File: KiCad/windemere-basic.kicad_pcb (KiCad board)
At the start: 2 copper layers, 246.4 x 157.5 mm, 51 parts, among them J2 Barrel_Jack, SW1 SW_SPDT, SW2 Push_Button, U1 WD65C02, U2 28C256, U3 62256, U4 WD65C22, U5 HD44780U, U6 74HC00, U7 MM74C922, U8 L7805, X1 1MHz

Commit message: pcb
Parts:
- R7: footprint Resistor_THT:R_Axial_DIN0207_L6.3mm_D2.5mm_P10.16mm_Horizontal -> Resistor_THT:R_Axial_DIN0204_L3.6mm_D1.6mm_P7.62mm_Horizontal
- SW1: footprint Button_Switch_THT:SW_DIP_SPSTx01_Slide_9.78x4.72mm_W7.62mm_P2.54mm -> Button_Switch_THT:SW_CuK_OS102011MA1QN1_SPDT_Angled
- U1: footprint 6502-Build:DIP-40_6502 -> Package_DIP:DIP-40_W15.24mm
- moved D5 128.5 mm to (173.5, 40.6)
- moved R7 120.5 mm to (161.2, 37.5)
- moved C1 120.2 mm to (174.0, 45.7)
- moved C4 119.4 mm to (147.3, 55.9)
- moved D6 119.3 mm to (134.6, 55.9)
- moved SW1 119.3 mm to (152.4, 48.3)
- moved C2 107.2 mm to (157.5, 188.0)
- moved C3 107.2 mm to (150.5, 188.0)
- moved SW2 102.9 mm to (161.3, 45.7)
- moved U8 100.5 mm to (124.5, 57.5)
- moved U2 82.6 mm to (155.5, 123.7)
- moved J2 75.8 mm to (140.7, 51.7)
- moved U6 68.8 mm to (152.8, 164.3)
- moved U3 52.7 mm to (137.1, 123.7)
- moved R1 46.9 mm to (163.8, 55.9)
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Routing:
- net Net-(R1-Pad1): track 0.00 -> 34.0 mm
- net Net-(C4-Pad1): track 0.00 -> 25.8 mm
- net Net-(RV1-Pad2): track 0.00 -> 23.1 mm
- net Net-(J2-Pad1): track 0.00 -> 14.0 mm
- net Net-(D6-Pad2): track 0.00 -> 11.7 mm
- added copper zone on In1.Cu, net +5V
- added copper zone on In2.Cu, net GND
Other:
- board size 246.4 x 157.5 mm -> 170.2 x 157.5 mm
- copper layers 2 -> 4

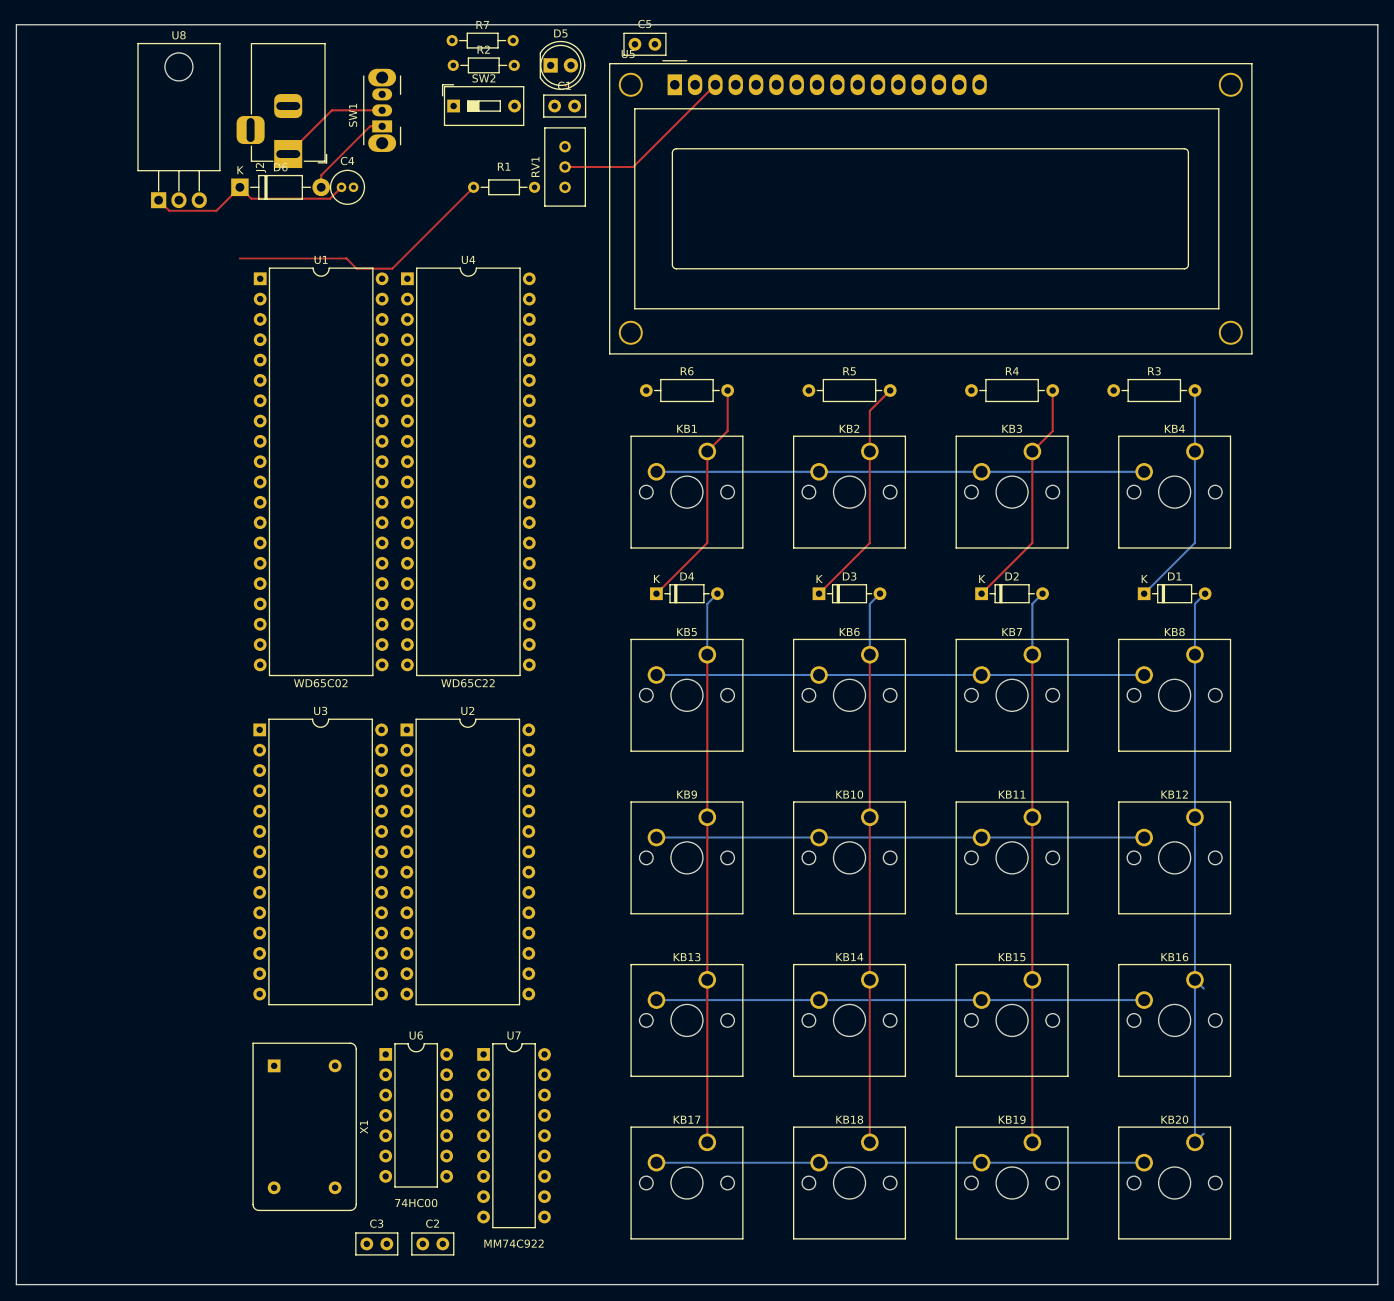
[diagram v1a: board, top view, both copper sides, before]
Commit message: footprint updates
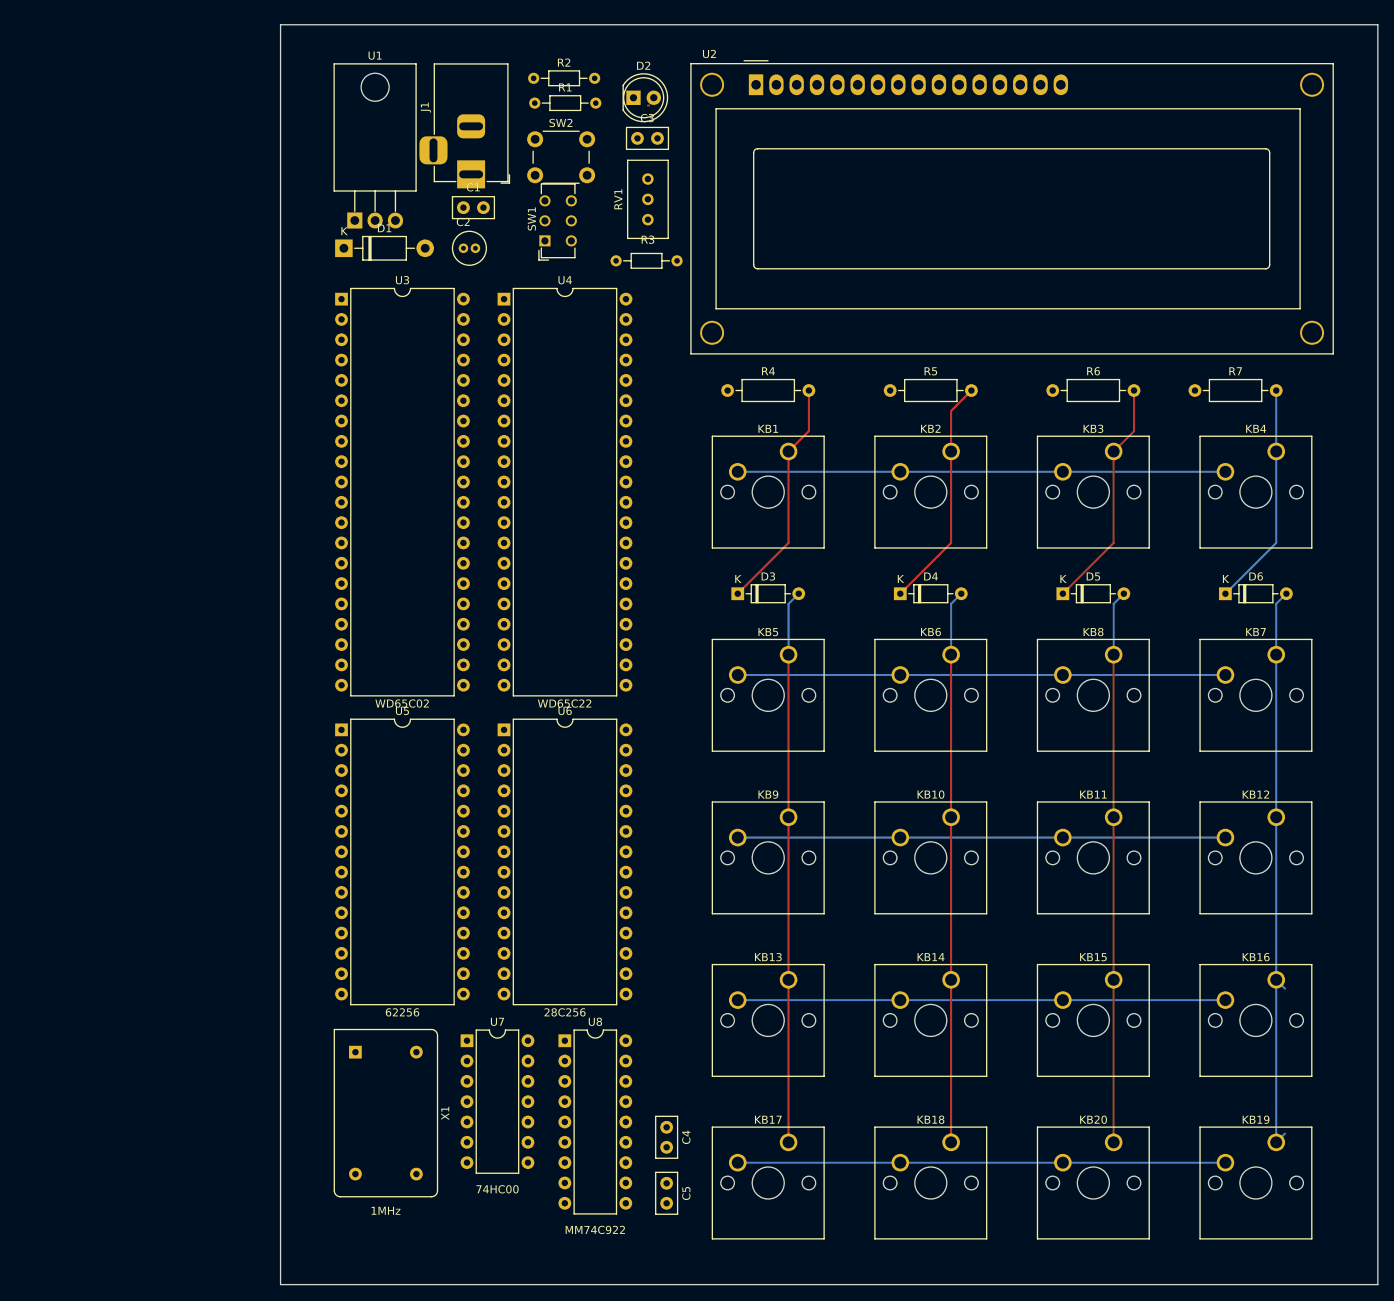
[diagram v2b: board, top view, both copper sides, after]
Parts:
- removed J2: Barrel_Jack, Connector_BarrelJack:BarrelJack_Horizontal
- added J1: Barrel_Jack, Connector_BarrelJack:BarrelJack_Horizontal, F.Cu at (163.5, 54.3)
- SW1: footprint Button_Switch_THT:SW_CuK_OS102011MA1QN1_SPDT_Angled -> Button_Switch_THT:SW_CuK_JS202011CQN_DPDT_Straight
- SW2: footprint Button_Switch_THT:SW_DIP_SPSTx01_Slide_9.78x4.72mm_W7.62mm_P2.54mm -> Button_Switch_THT:SW_PUSH_6mm_H4.3mm
- moved C4 40.2 mm to (188.0, 173.4), turned to -90 degrees
- moved C5 31.4 mm to (188.0, 180.4), turned to -90 degrees
- moved C1 29.6 mm to (162.6, 58.4)
- moved SW1 24.9 mm to (172.7, 62.6)
- moved U1 24.7 mm to (149.0, 60.0)
- moved R3 20.0 mm to (181.6, 65.1)
- moved C2 17.0 mm to (162.6, 63.5)
- moved D1 15.1 mm to (147.6, 63.5)
- moved U4 12.3 mm to (167.6, 69.9)
- moved U6 12.1 mm to (167.6, 123.7)
- moved R1 11.2 mm to (171.5, 45.4)
- moved R2 11.2 mm to (171.3, 42.3)
- moved RV1 11.1 mm to (185.6, 54.8)
- moved C3 11.1 mm to (184.3, 49.8)
- moved D2 11.1 mm to (183.8, 44.7)
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- renumbered C5 to C1, C4 to C2, C1 to C3, C3 to C4, C2 to C5, D6 to D1, D5 to D2, D4 to D3, D3 to D4, D2 to D5, D1 to D6, KB20 to KB19, KB19 to KB20, KB8 to KB7, KB7 to KB8, R2 to R1, R7 to R2, R1 to R3, R6 to R4, R4 to R6, R3 to R7, U8 to U1, U5 to U2, U1 to U3, U3 to U5, U2 to U6, U6 to U7, U7 to U8
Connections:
- C1 pad 1: +5V -> Net-(C1-Pad1)
- C2 pad 1: Net-(C4-Pad1) -> Net-(C2-Pad1)
- C3 pad 1: Net-(C1-Pad1) -> Net-(C3-Pad1)
- C4 pad 1: Net-(C3-Pad1) -> Net-(C4-Pad1)
- C5 pad 1: Net-(C2-Pad1) -> +5V
- D1 pad 1: Net-(C4-Pad1) -> Net-(D1-Pad1)
- D1 pad 2: Net-(D6-Pad2) -> Net-(D1-Pad2)
- D2 pad 1: Net-(D5-Pad1) -> Net-(D2-Pad1)
- D2 pad 2: +5V -> Net-(D2-Pad2)
- D3 pad 1: Net-(D4-Pad1) -> Net-(D3-Pad1)
- D3 pad 2: Net-(D4-Pad2) -> Net-(D3-Pad2)
- D4 pad 1: Net-(D3-Pad1) -> Net-(D4-Pad1)
- D4 pad 2: Net-(D3-Pad2) -> Net-(D4-Pad2)
- D5 pad 1: Net-(D2-Pad1) -> Net-(D5-Pad1)
- D5 pad 2: Net-(D2-Pad2) -> +5V
- D6 pad 1: Net-(D1-Pad1) -> Net-(C4-Pad1)
- D6 pad 2: Net-(D1-Pad2) -> Net-(D6-Pad2)
- KB19 pad 1: Net-(D1-Pad2) -> Net-(D2-Pad2)
- KB20 pad 1: Net-(D2-Pad2) -> Net-(D1-Pad2)
- KB7 pad 1: Net-(D1-Pad2) -> Net-(D2-Pad2)
- KB8 pad 1: Net-(D2-Pad2) -> Net-(D1-Pad2)
- R1 pad 1: +5V -> Net-(R1-Pad1)
- R1 pad 2: Net-(C1-Pad1) -> +5V
- R2 pad 1: Net-(D5-Pad1) -> +5V
- R2 pad 2: GND -> Net-(C1-Pad1)
- R3 pad 1: Net-(R1-Pad1) -> +5V
- R3 pad 2: +5V -> Net-(D1-Pad1)
- R4 pad 2: Net-(D4-Pad1) -> Net-(D2-Pad1)
- R6 pad 2: Net-(D2-Pad1) -> Net-(D4-Pad1)
- R7 pad 1: +5V -> Net-(D5-Pad1)
- R7 pad 2: Net-(D1-Pad1) -> GND
- U1 pad 1: Net-(C4-Pad1) -> unconnected-(U1-Pad1)
- U1 pad 2: GND -> Net-(R1-Pad1)
- U1 pad 3: +5V -> unconnected-(U1-Pad3)
- U2 pad 1: GND -> /A14
- U2 pad 10: Net-(U4-Pad13) -> /A0
- U2 pad 11: Net-(U4-Pad14) -> /D0
- U2 pad 12: Net-(U4-Pad15) -> /D1
- U2 pad 13: Net-(U4-Pad16) -> /D2
- U2 pad 14: Net-(U4-Pad17) -> GND
- U2 pad 15: +5V -> /D3
- U2 pad 16: GND -> /D4
- U2 pad 2: +5V -> /A12
- U2 pad 3: Net-(RV1-Pad2) -> /A7
- U2 pad 4: Net-(U4-Pad7) -> /A6
- U2 pad 5: Net-(U4-Pad8) -> /A5
- U2 pad 6: Net-(U4-Pad9) -> /A4
- U2 pad 7: Net-(U4-Pad10) -> /A3
- U2 pad 8: Net-(U4-Pad11) -> /A2
- U2 pad 9: Net-(U4-Pad12) -> /A1
- U3 pad 1: unconnected-(U1-Pad1) -> /A14
- U3 pad 10: /A1 -> /A0
- U3 pad 11: /A2 -> /D0
- U3 pad 12: /A3 -> /D1
- U3 pad 13: /A4 -> /D2
- U3 pad 14: /A5 -> GND
- U3 pad 15: /A6 -> /D3
- U3 pad 16: /A7 -> /D4
- U3 pad 17: /A8 -> /D5
- U3 pad 18: /A9 -> /D6
- U3 pad 19: /A10 -> /D7
- U3 pad 2: Net-(R1-Pad1) -> /A12
- U3 pad 20: /A11 -> Net-(U3-Pad20)
- U3 pad 21: GND -> /A10
- U3 pad 22: /A12 -> /A14
- U3 pad 23: /A13 -> /A11
- U3 pad 24: /A14 -> /A9
- U3 pad 25: /A15 -> /A8
- U3 pad 26: /D7 -> /A13
- U3 pad 27: /D6 -> Net-(U1-Pad34)
- U3 pad 28: /D5 -> +5V
- U3 pad 29: /D4 -> (no net)
- U3 pad 3: unconnected-(U1-Pad3) -> /A7
- U3 pad 30: /D3 -> (no net)
- U3 pad 31: /D2 -> (no net)
- U3 pad 32: /D1 -> (no net)
- U3 pad 33: /D0 -> (no net)
- U3 pad 34: Net-(U1-Pad34) -> (no net)
- U3 pad 35: unconnected-(U1-Pad35) -> (no net)
- U3 pad 36: +5V -> (no net)
- U3 pad 37: Net-(U1-Pad37) -> (no net)
- U3 pad 38: unconnected-(U1-Pad38) -> (no net)
- U3 pad 39: unconnected-(U1-Pad39) -> (no net)
- U3 pad 4: Net-(U1-Pad4) -> /A6
- U3 pad 40: Net-(C1-Pad1) -> (no net)
- U3 pad 5: unconnected-(U1-Pad5) -> /A5
- U3 pad 6: +5V -> /A4
- U3 pad 7: unconnected-(U1-Pad7) -> /A3
- U3 pad 8: +5V -> /A2
- U3 pad 9: /A0 -> /A1
- U5 pad 1: /A14 -> GND
- U5 pad 10: /A0 -> Net-(U4-Pad13)
- U5 pad 11: /D0 -> Net-(U4-Pad14)
- U5 pad 12: /D1 -> Net-(U4-Pad15)
- U5 pad 13: /D2 -> Net-(U4-Pad16)
- U5 pad 14: GND -> Net-(U4-Pad17)
- U5 pad 15: /D3 -> +5V
- U5 pad 16: /D4 -> GND
- U5 pad 17: /D5 -> (no net)
- U5 pad 18: /D6 -> (no net)
- U5 pad 19: /D7 -> (no net)
- U5 pad 2: /A12 -> +5V
- U5 pad 20: Net-(U3-Pad20) -> (no net)
- U5 pad 21: /A10 -> (no net)
- U5 pad 22: /A14 -> (no net)
- U5 pad 23: /A11 -> (no net)
- U5 pad 24: /A9 -> (no net)
- U5 pad 25: /A8 -> (no net)
- U5 pad 26: /A13 -> (no net)
- U5 pad 27: Net-(U1-Pad34) -> (no net)
- U5 pad 28: +5V -> (no net)
- U5 pad 3: /A7 -> Net-(RV1-Pad2)
- U5 pad 4: /A6 -> Net-(U4-Pad7)
- U5 pad 5: /A5 -> Net-(U4-Pad8)
- U5 pad 6: /A4 -> Net-(U4-Pad9)
- U5 pad 7: /A3 -> Net-(U4-Pad10)
- U5 pad 8: /A2 -> Net-(U4-Pad11)
- U5 pad 9: /A1 -> Net-(U4-Pad12)
- U6 pad 1: /A14 -> /A15
- U6 pad 10: /A0 -> Net-(U2-Pad20)
- U6 pad 11: /D0 -> Net-(U6-Pad11)
- U6 pad 12: /D1 -> Net-(U4-Pad40)
- U6 pad 13: /D2 -> Net-(U1-Pad37)
- U6 pad 14: GND -> +5V
- U6 pad 15: /D3 -> (no net)
- U6 pad 16: /D4 -> (no net)
- U6 pad 17: /D5 -> (no net)
- U6 pad 18: /D6 -> (no net)
- U6 pad 19: /D7 -> (no net)
- U6 pad 2: /A12 -> /A15
- U6 pad 20: Net-(U2-Pad20) -> (no net)
- U6 pad 21: /A10 -> (no net)
- U6 pad 22: GND -> (no net)
- U6 pad 23: /A11 -> (no net)
- U6 pad 24: /A9 -> (no net)
- U6 pad 25: /A8 -> (no net)
- U6 pad 26: /A13 -> (no net)
- U6 pad 27: +5V -> (no net)
- U6 pad 28: +5V -> (no net)
- U6 pad 3: /A7 -> Net-(U2-Pad20)
- U6 pad 4: /A6 -> Net-(U1-Pad37)
- U6 pad 5: /A5 -> Net-(U2-Pad20)
- U6 pad 6: /A4 -> Net-(U3-Pad20)
- U6 pad 7: /A3 -> GND
- U6 pad 8: /A2 -> Net-(U4-Pad23)
- U6 pad 9: /A1 -> /A14
- U7 pad 1: /A15 -> Net-(D1-Pad2)
- U7 pad 10: Net-(U2-Pad20) -> Net-(KB10-Pad2)
- U7 pad 11: Net-(U6-Pad11) -> Net-(KB5-Pad2)
- U7 pad 13: Net-(U1-Pad37) -> Net-(U6-Pad11)
- U7 pad 14: +5V -> Net-(U4-Pad5)
- U7 pad 2: /A15 -> Net-(D2-Pad2)
- U7 pad 3: Net-(U2-Pad20) -> Net-(D3-Pad2)
- U7 pad 4: Net-(U1-Pad37) -> Net-(D4-Pad2)
- U7 pad 5: Net-(U2-Pad20) -> Net-(C3-Pad1)
- U7 pad 6: Net-(U3-Pad20) -> Net-(C2-Pad1)
- U7 pad 7: GND -> Net-(KB17-Pad2)
- U7 pad 8: Net-(U4-Pad23) -> Net-(KB13-Pad2)
- U7 pad 9: /A14 -> GND
- U8 pad 1: Net-(D1-Pad2) -> Net-(C4-Pad1)
- U8 pad 10: Net-(KB10-Pad2) -> (no net)
- U8 pad 11: Net-(KB5-Pad2) -> (no net)
- U8 pad 12: Net-(U4-Pad40) -> (no net)
- U8 pad 13: Net-(U6-Pad11) -> (no net)
- U8 pad 14: Net-(U4-Pad5) -> (no net)
- U8 pad 15: Net-(U4-Pad4) -> (no net)
- U8 pad 16: Net-(U4-Pad3) -> (no net)
- U8 pad 17: Net-(U4-Pad2) -> (no net)
- U8 pad 18: +5V -> (no net)
- U8 pad 2: Net-(D2-Pad2) -> GND
- U8 pad 3: Net-(D3-Pad2) -> +5V
- U8 pad 4: Net-(D4-Pad2) -> (no net)
- U8 pad 5: Net-(C3-Pad1) -> (no net)
- U8 pad 6: Net-(C2-Pad1) -> (no net)
- U8 pad 7: Net-(KB17-Pad2) -> (no net)
- U8 pad 8: Net-(KB13-Pad2) -> (no net)
- U8 pad 9: GND -> (no net)
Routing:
- net Net-(R1-Pad1): track 34.0 -> 0.00 mm
- net Net-(D3-Pad1): track 29.1 -> 58.2 mm
- net Net-(D4-Pad1): track 29.1 -> 0.00 mm
- net GND: track 0.00 -> 28.0 mm
- net Net-(D1-Pad1): track 28.0 -> 0.00 mm
- net Net-(C4-Pad1): track 25.8 -> 0.00 mm
- net Net-(RV1-Pad2): track 23.1 -> 0.00 mm
- net Net-(SW1-Pad2): track 14.0 -> 0.00 mm
- net Net-(D6-Pad2): track 11.7 -> 0.00 mm
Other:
- board size 170.2 x 157.5 mm -> 137.2 x 157.5 mm

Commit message: correct issues
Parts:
- removed the C4 at (188.0, 173.4)
- removed the D5 at (237.5, 106.7)
- removed the D6 at (257.8, 106.7)
- removed the KB18 at (223.5, 175.3)
- removed the R6 at (236.2, 81.3)
- removed the SW1 at (172.7, 62.6)
- added C2: 0.1uF, Capacitor_THT:C_Disc_D5.0mm_W2.5mm_P2.50mm, F.Cu at (172.3, 174.8)
- added C6: 0.1µF, Capacitor_THT:C_Disc_D5.0mm_W2.5mm_P2.50mm, F.Cu at (153.7, 65.5)
- added D1: LED, LED_THT:LED_D5.0mm, F.Cu at (184.2, 44.8)
- added D2: 1N5819, Diode_THT:D_DO-41_SOD81_P10.16mm_Horizontal, F.Cu at (159.6, 65.4)
- added KB15: Push_Button, Button_Switch_Keyboard:SW_Cherry_MX_1.00u_PCB, F.Cu at (223.5, 175.3)
- added R5: 100K, Resistor_THT:R_Axial_DIN0207_L6.3mm_D2.5mm_P10.16mm_Horizontal, F.Cu at (236.2, 81.3)
- added REF1: MountingHole_3.2mm_M3_DIN965_Pad_TopBottom, MountingHole:MountingHole_3.2mm_M3_DIN965_Pad_TopBottom, F.Cu at (142.2, 41.9)
- added REF2: MountingHole_3.2mm_M3_DIN965_Pad_TopBottom, MountingHole:MountingHole_3.2mm_M3_DIN965_Pad_TopBottom, F.Cu at (275.6, 41.9)
- added REF3: MountingHole_3.2mm_M3_DIN965_Pad_TopBottom, MountingHole:MountingHole_3.2mm_M3_DIN965_Pad_TopBottom, F.Cu at (142.2, 186.7)
- added REF4: MountingHole_3.2mm_M3_DIN965_Pad_TopBottom, MountingHole:MountingHole_3.2mm_M3_DIN965_Pad_TopBottom, F.Cu at (275.6, 186.7)
- added REF?: MountingHole_3.2mm_M3, MountingHole:MountingHole_3.2mm_M3, F.Cu at (188.0, 111.8)
- added SW2: SW_SPDT, Button_Switch_THT:SW_E-Switch_EG1271_DPDT, F.Cu at (172.6, 59.2)
- C1: value 0.1µF -> 1uF
- C3: renamed from C2; value 1µF -> 1uF; footprint Capacitor_THT:C_Radial_D4.0mm_H7.0mm_P1.50mm -> Capacitor_THT:C_Disc_D5.0mm_W2.5mm_P2.50mm
- C4: renamed from C3; value 1uF -> 0.1uF
- C5: value 1uF -> 1µF; footprint Capacitor_THT:C_Disc_D5.0mm_W2.5mm_P2.50mm -> Capacitor_THT:C_Radial_D4.0mm_H7.0mm_P1.50mm
- D3: renamed from D1; value 1N5819 -> 1N914; footprint Diode_THT:D_DO-41_SOD81_P10.16mm_Horizontal -> Diode_THT:D_DO-35_SOD27_P7.62mm_Horizontal
- D4: renamed from D2; value LED -> 1N914; footprint LED_THT:LED_D5.0mm -> Diode_THT:D_DO-35_SOD27_P7.62mm_Horizontal
- R1: renamed from R2; value 1k -> 1K
- R3: value 1K -> 1k
- SW1: renamed from SW2; footprint Button_Switch_THT:SW_PUSH_6mm_H4.3mm -> Button_Switch_THT:SW_PUSH_6mm
- U1: renamed from U5; value 62256 -> HD44780U; footprint Package_DIP:DIP-28_W15.24mm -> Display:WC1602A
- U2: renamed from U1; value L7805 -> WD65C02; footprint Package_TO_SOT_THT:TO-220-3_Horizontal_TabDown -> Package_DIP:DIP-40_W15.24mm
- U3: renamed from U2; value HD44780U -> 28C256; footprint Display:WC1602A -> Package_DIP:DIP-28_W15.24mm
- U4: renamed from U3; value WD65C02 -> 62256; footprint Package_DIP:DIP-40_W15.24mm -> Package_DIP:DIP-28_W15.24mm
- U6: value 28C256 -> 74HC00; footprint Package_DIP:DIP-28_W15.24mm -> Package_DIP:DIP-14_W7.62mm
- U7: value 74HC00 -> MM74C922; footprint Package_DIP:DIP-14_W7.62mm -> Package_DIP:DIP-18_W7.62mm
- U8: value MM74C922 -> L7805; footprint Package_DIP:DIP-18_W7.62mm -> Package_TO_SOT_THT:TO-220-3_Horizontal_TabDown
- moved C4 136.8 mm to (172.3, 186.0), turned to 90 degrees
- moved C5 121.4 mm to (148.7, 65.5), turned to 0 degrees
- moved D3 118.3 mm to (257.8, 106.7)
- moved C3 114.8 mm to (172.3, 177.9), turned to -90 degrees
- moved U8 105.2 mm to (149.7, 60.5)
- moved U3 97.6 mm to (147.3, 125.7)
- moved U1 95.9 mm to (199.1, 43.1)
- moved D4 82.0 mm to (237.5, 106.7)
- moved R4 61.0 mm to (256.5, 81.3)
- moved U4 59.5 mm to (167.6, 125.7)
- moved R7 58.4 mm to (195.6, 81.3)
- moved U6 47.6 mm to (175.2, 170.7)
- moved R3 25.4 mm to (171.4, 41.8)
- moved KB10 20.3 mm to (243.8, 175.3)
- moved KB2 20.3 mm to (264.2, 114.3)
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- renumbered D3 to D5, D4 to D6, KB4 to KB1, KB19 to KB10, KB2 to KB11, KB6 to KB12, KB10 to KB13, KB1 to KB16, KB5 to KB17, KB9 to KB18, KB13 to KB19, KB8 to KB2, KB17 to KB20, KB12 to KB3, KB16 to KB4, KB20 to KB5, KB3 to KB6, KB11 to KB8, KB15 to KB9, R1 to R2, R5 to R6, U4 to U5
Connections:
- C5 pad 1: +5V -> Net-(C5-Pad1)
- D3 pad 1: Net-(D1-Pad1) -> Net-(D3-Pad1)
- D4 pad 1: Net-(D2-Pad1) -> Net-(D4-Pad1)
- D6 pad 1: Net-(D4-Pad1) -> Net-(D6-Pad1)
- KB1 pad 1: Net-(D1-Pad1) -> Net-(D3-Pad1)
- KB16 pad 1: Net-(D4-Pad1) -> Net-(D6-Pad1)
- KB6 pad 1: Net-(D2-Pad1) -> Net-(D4-Pad1)
- R3 pad 1: +5V -> Net-(D1-Pad1)
- R3 pad 2: Net-(D1-Pad1) -> GND
- R4 pad 2: Net-(D2-Pad1) -> Net-(D3-Pad1)
- R7 pad 1: Net-(D5-Pad1) (its old number) -> +5V
- R7 pad 2: GND -> Net-(D6-Pad1)
- U4 pad 27: Net-(U1-Pad34) -> Net-(U2-Pad34)
- U5 pad 2: Net-(U4-Pad2) -> Net-(U5-Pad2)
- U5 pad 21: Net-(U1-Pad4) (its old number) -> Net-(U2-Pad4)
- U5 pad 22: Net-(U1-Pad34) -> Net-(U2-Pad34)
- U5 pad 25: Net-(U1-Pad37) -> Net-(U2-Pad37)
- U5 pad 3: Net-(U4-Pad3) -> Net-(U5-Pad3)
- U5 pad 4: Net-(U4-Pad4) -> Net-(U5-Pad4)
- U5 pad 40: Net-(U4-Pad40) -> Net-(U5-Pad40)
- U6 pad 10: Net-(U2-Pad20) -> Net-(U3-Pad20)
- U6 pad 11: Net-(U6-Pad11) -> (no net)
- U6 pad 12: Net-(U4-Pad40) -> (no net)
- U6 pad 13: Net-(U1-Pad37) -> (no net)
- U6 pad 3: Net-(U2-Pad20) -> Net-(U3-Pad20)
- U6 pad 4: Net-(U1-Pad37) -> Net-(U2-Pad37)
- U6 pad 5: Net-(U2-Pad20) -> Net-(U3-Pad20)
- U7 pad 12: Net-(U4-Pad40) -> Net-(U5-Pad40)
- U7 pad 13: Net-(U6-Pad11) -> GND
- U8 pad 1: Net-(C4-Pad1) (its old number) -> Net-(C5-Pad1)
- X1 pad 8: Net-(U1-Pad37) -> Net-(U2-Pad37)
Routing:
- net +5V: track 0.00 -> 386.1 mm
- net /D1: track 0.00 -> 144.4 mm
- net Net-(U5-Pad3): track 0.00 -> 140.8 mm
- net Net-(U5-Pad40): track 0.00 -> 140.3 mm
- net Net-(U5-Pad4): track 0.00 -> 140.2 mm, vias 0 -> 1
- net Net-(U2-Pad37): track 0.00 -> 135.5 mm
- net Net-(U5-Pad2): track 0.00 -> 132.8 mm
- net /D0: track 0.00 -> 128.9 mm
- net /A1: track 0.00 -> 127.7 mm, vias 0 -> 1
- net /A0: track 0.00 -> 124.5 mm
- net Net-(U1-Pad8): track 0.00 -> 123.4 mm
- net Net-(U5-Pad5): track 0.00 -> 120.6 mm, vias 0 -> 1
- net /A2: track 0.00 -> 113.6 mm
- net /D2: track 0.00 -> 112.3 mm
- net /D3: track 0.00 -> 111.5 mm
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- added copper zone on B.Cu, net GND
- removed copper zone on In1.Cu, net +5V
- removed copper zone on In2.Cu, net GND
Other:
- board size 137.2 x 157.5 mm -> 146.1 x 157.5 mm
- copper layers 4 -> 2
